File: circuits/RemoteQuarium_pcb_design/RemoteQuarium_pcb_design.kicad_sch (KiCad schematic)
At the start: 53 parts, among them J1 Power_terminal, J10 LCD_pins, J11 Servo pins, J12 ESP_pins, J13 PH_sensor_sockets, J14 Ph_sesnor-pins, J15 Power & RX-TX, J16 Reset_button_terminal, J2 ESP left side sockets, J3 ESP right side sockets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

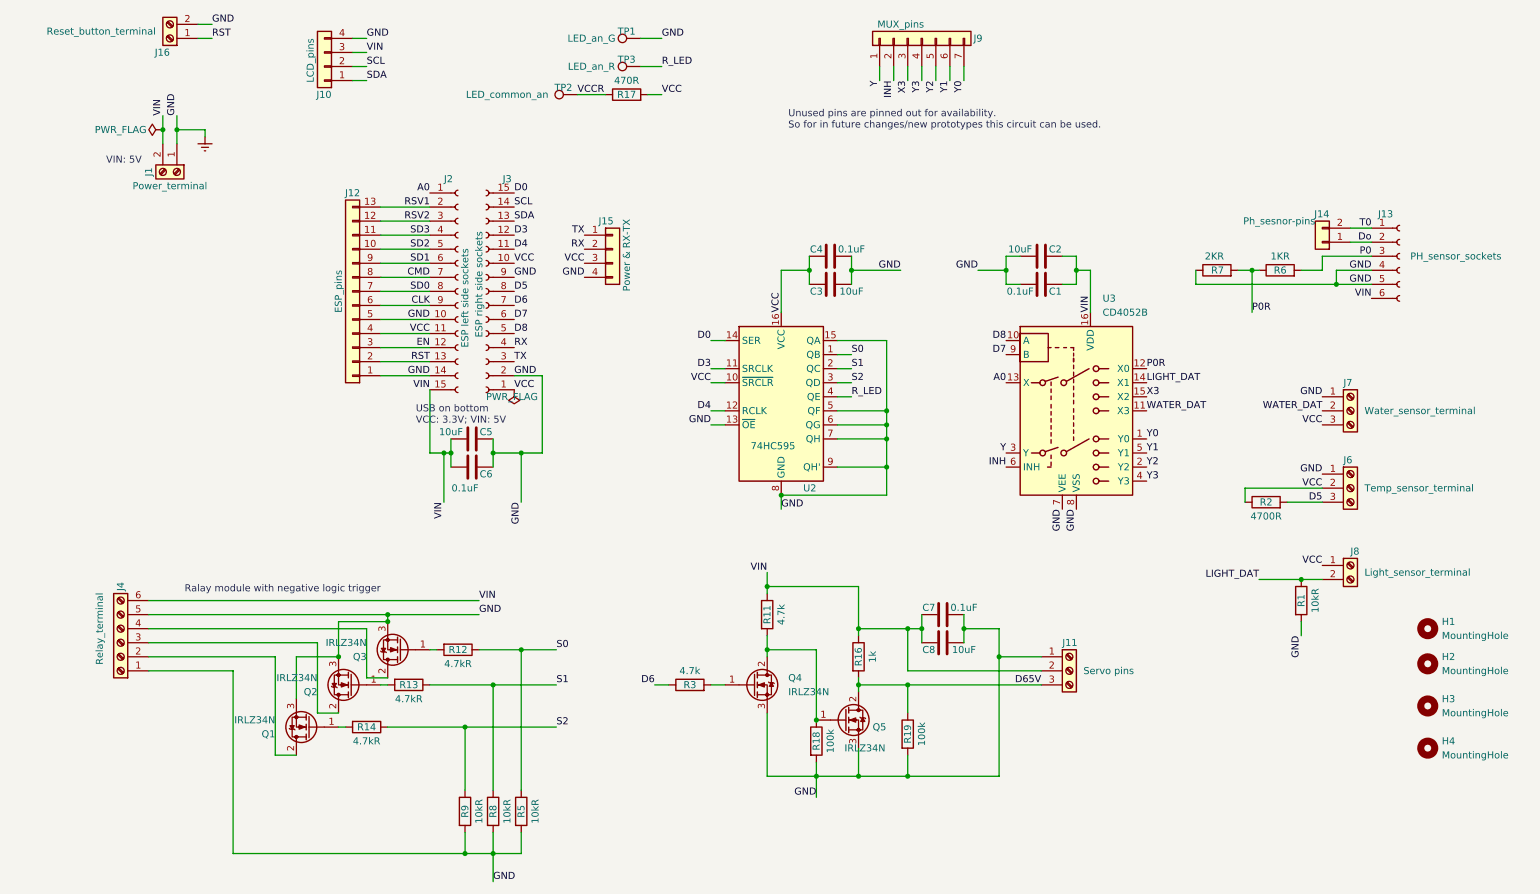
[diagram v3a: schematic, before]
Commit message: Fixed user email change issue
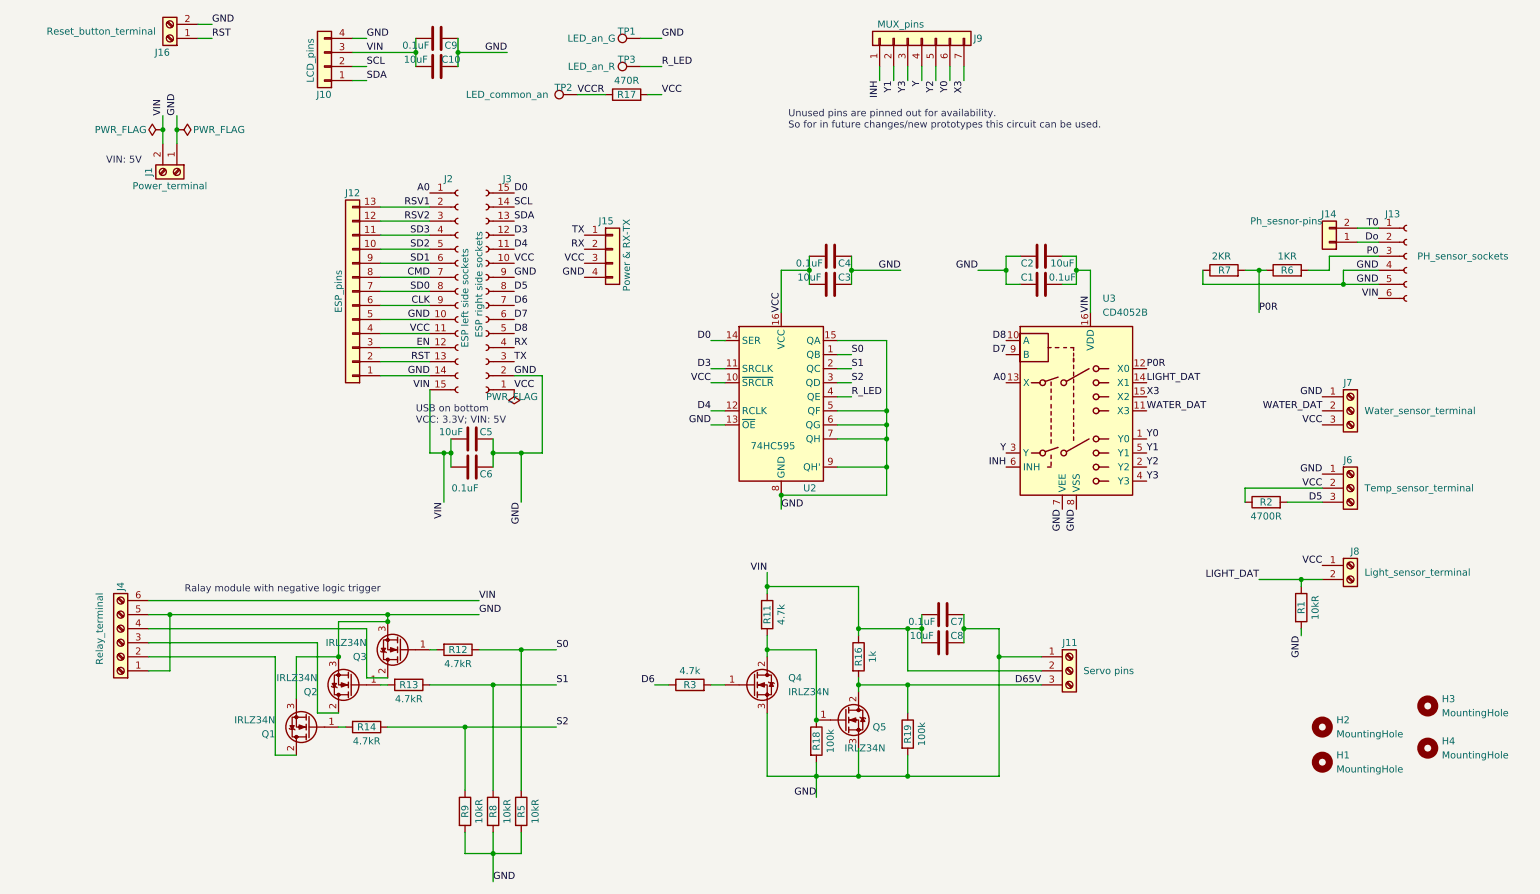
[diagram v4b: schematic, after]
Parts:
- added C10: 10uF, Capacitor_THT:CP_Radial_D6.3mm_P2.50mm, symbol Device:C
- added C9: 0.1uF, Capacitor_THT:CP_Radial_D6.3mm_P2.50mm, symbol Device:C
- C1, C4, C6, C7: footprint Capacitor_THT:CP_Radial_D4.0mm_P1.50mm -> Capacitor_THT:CP_Radial_D6.3mm_P2.50mm
- J16: footprint NXW:NXW-02P -> TerminalBlock_Phoenix:TerminalBlock_Phoenix_MPT-0,5-2-2.54_1x02_P2.54mm_Horizontal
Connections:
- net INH: now also J9.1 (Pin_1); no longer J9.2 (Pin_2)
- net VCC: now also C3.1, C4.1; no longer C3.2, C4.2
- net VIN: now also C1.1, C2.1, C7.1, C8.1, C10.1, C9.1; no longer C1.2, C2.2, C7.2, C8.2
- net X3: now also J9.7 (Pin_7); no longer J9.3 (Pin_3)
- net Y: now also J9.4 (Pin_4); no longer J9.1 (Pin_1)
- net Y0: now also J9.6 (Pin_6); no longer J9.7 (Pin_7)
- net Y1: now also J9.2 (Pin_2); no longer J9.6 (Pin_6)
- net Y3: now also J9.3 (Pin_3); no longer J9.4 (Pin_4)
- net Earth renamed GND
- net GND: now also C1.2, C2.2, C3.2, C4.2, C7.2, C8.2, C10.2, C9.2; no longer C1.1, C2.1, C3.1, C4.1, C7.1, C8.1
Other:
- moved on the sheet: C1, C2, C3, C4, C7, C8, H1, H2, J13, J14, R1, R6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
